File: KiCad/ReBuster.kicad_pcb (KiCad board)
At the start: 4 copper layers, 38 x 38 mm, 37 parts, among them U1 10M02SCU169, U2 LM1117-3.3, U3 SN74CBTD16210, U4 SN74LVC16T245DGVR, U5 SN74CBTD16210, U6 SN74CBTD16210, U7 74LVC2T45DC, U8 PLCC_84_plug, U9 PLCC_84_plug

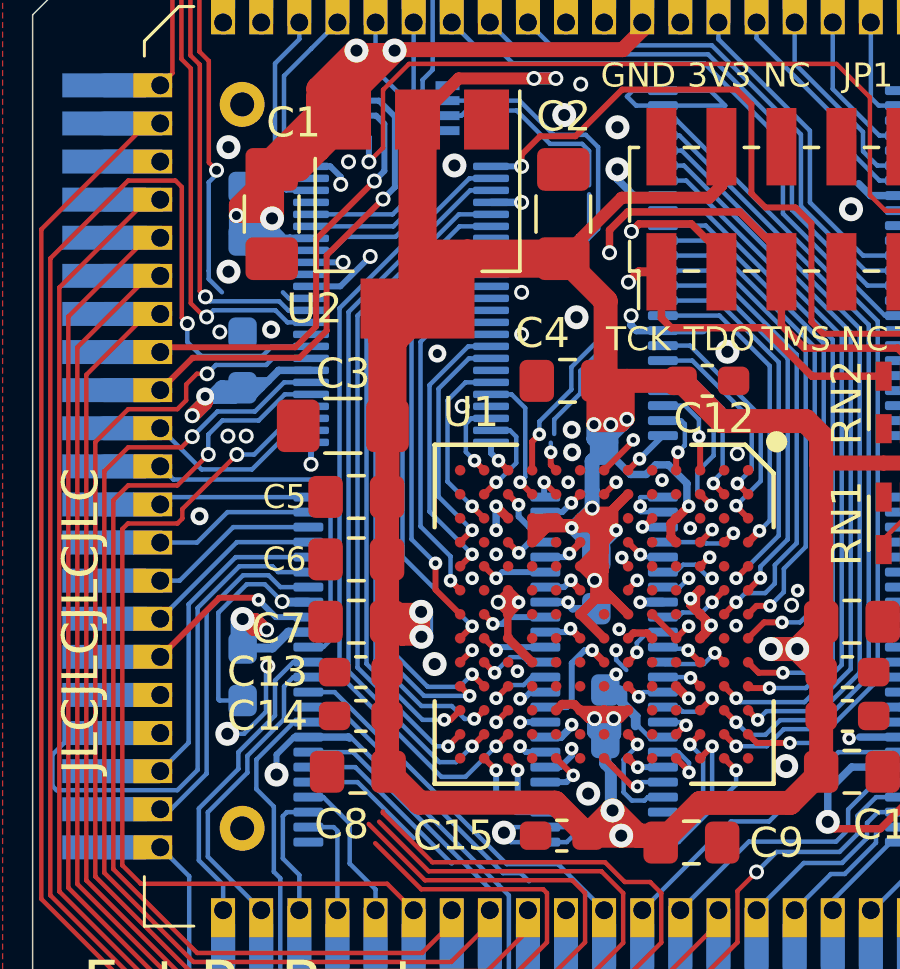
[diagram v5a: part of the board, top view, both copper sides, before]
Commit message: Route EDS0 to U4 (SN74LVC16T245DGVR) change F4 -> N8 in FPGA
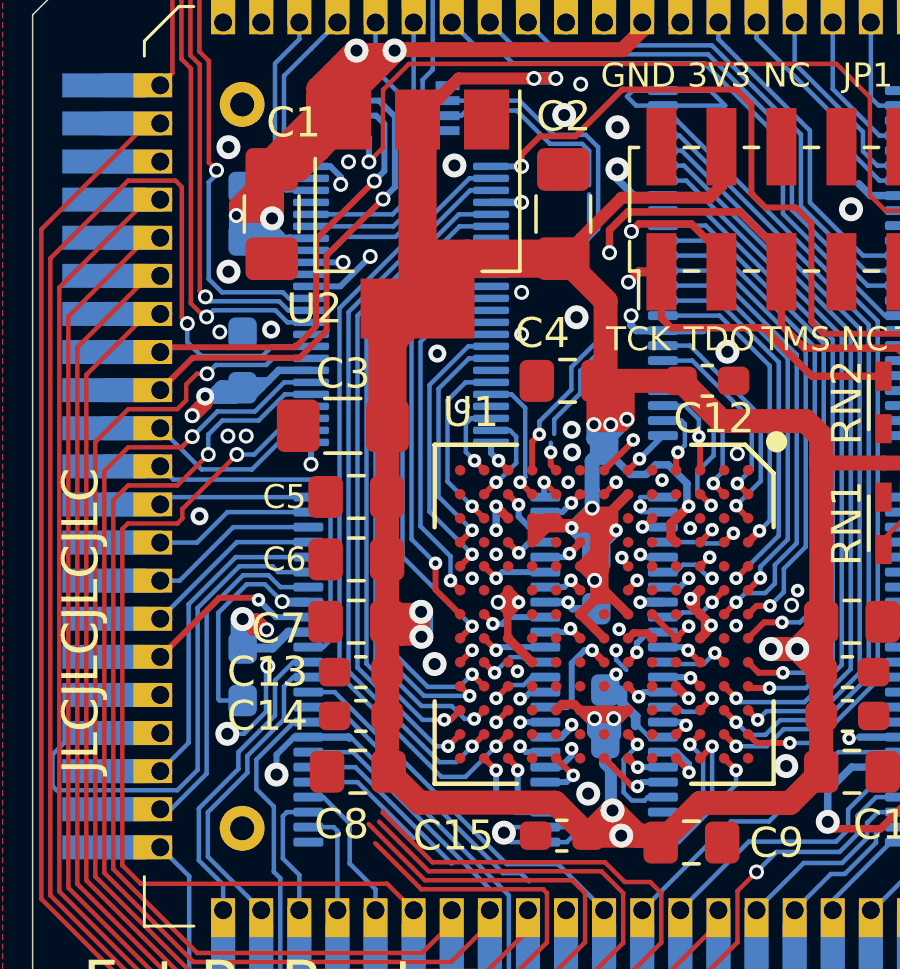
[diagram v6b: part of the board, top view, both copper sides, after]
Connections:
- U1 pad F4: EDS0_FPGA -> Net-(U1-PadF4)
- U1 pad N8: Net-(U1-PadN8) -> EDS0_FPGA
- U4 pad 13: Net-(U4-Pad13) -> EDS0
- U4 pad 36: Net-(U4-Pad36) -> EDS0_FPGA
- U5 pad 44: EDS0_FPGA -> Net-(U5-Pad44)
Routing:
- net Net-(U1-PadN8): track 13.9 -> 0.00 mm, vias 1 -> 0
- net EDS0_FPGA: track 1.36 -> 14.7 mm
- net EDS0: track 62.7 -> 65.7 mm
- net Net-(U4-Pad13): track 1.02 -> 0.00 mm
- net Net-(U5-Pad44): track 0.00 -> 0.79 mm, vias 0 -> 1

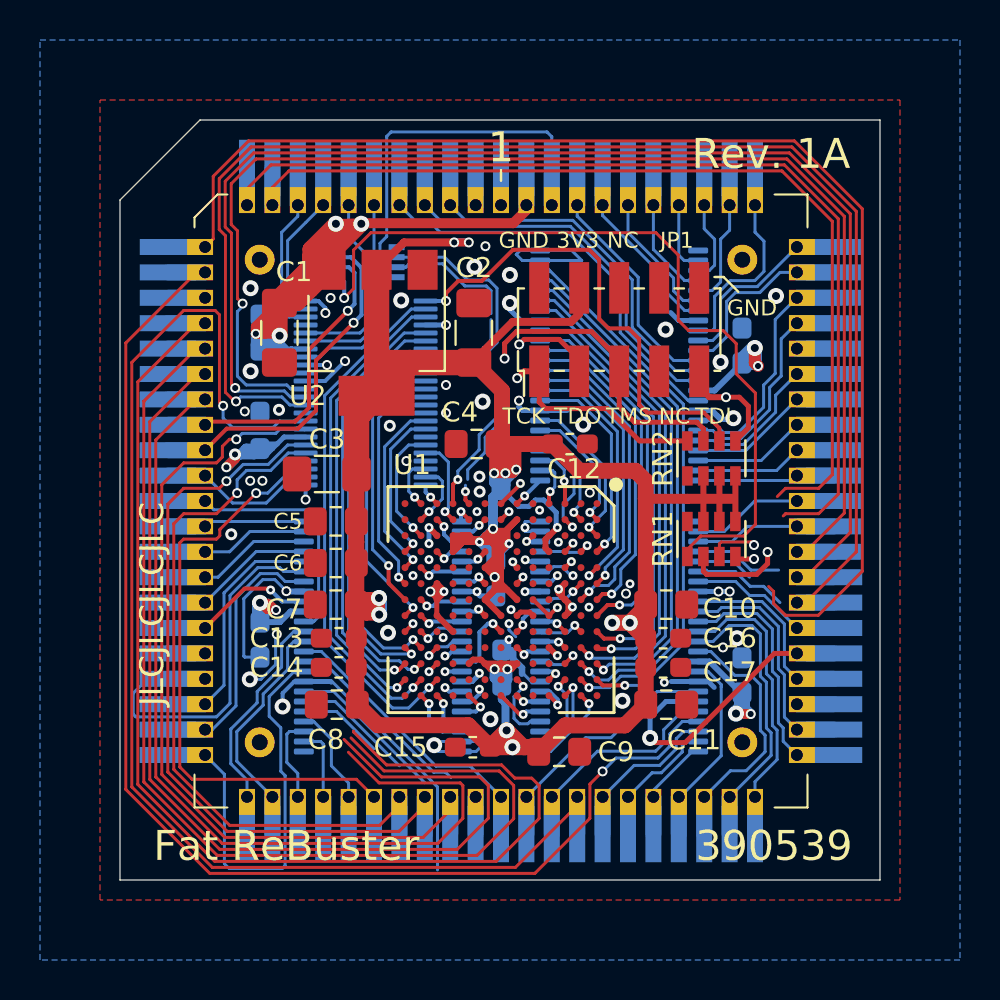
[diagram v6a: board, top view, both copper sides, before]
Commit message: Route RMC, SBR, SBG, CIIN to U6 (SN74CBTD16210) and assign pins K10, K11, K12, H13 in FPGA respectively
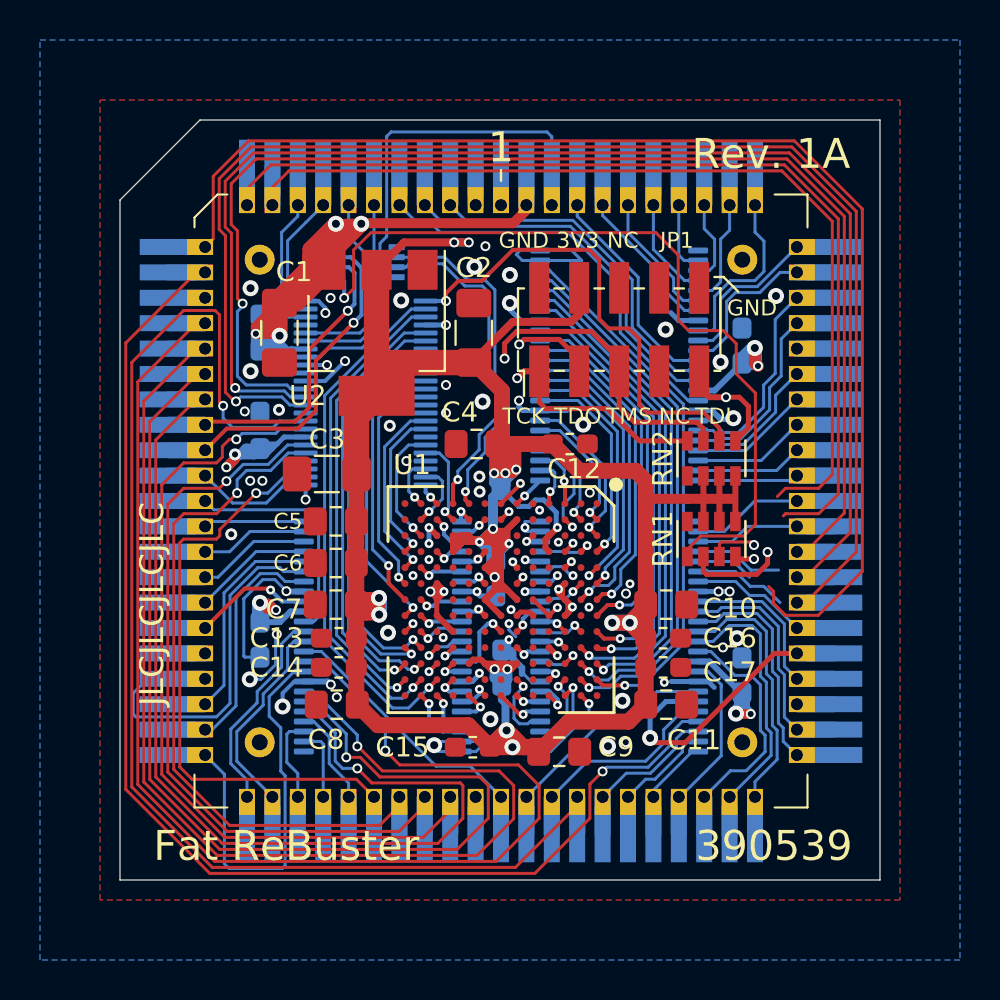
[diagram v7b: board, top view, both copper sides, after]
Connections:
- U1 pad H13: Net-(U1-PadH13) -> CIIN_FPGA
- U1 pad J1: Net-(U1-PadJ1) -> DTACK_FPGA
- U1 pad K1: Net-(U1-PadK1) -> MTACK_FPGA
- U1 pad K10: Net-(U1-PadK10) -> RMC_FPGA
- U1 pad K11: Net-(U1-PadK11) -> SBR_FPGA
- U1 pad K12: Net-(U1-PadK12) -> SBG_FPGA
- U6 pad 10: Net-(U6-Pad10) -> RMC
- U6 pad 38: Net-(U6-Pad38) -> RMC_FPGA
- U6 pad 40: Net-(U6-Pad40) -> SBR_FPGA
- U6 pad 42: Net-(U6-Pad42) -> SBG_FPGA
- U6 pad 43: Net-(U6-Pad43) -> CIIN_FPGA
- U6 pad 5: Net-(U6-Pad5) -> CIIN
- U6 pad 6: Net-(U6-Pad6) -> SBG
- U6 pad 7: Net-(U6-Pad7) -> SBR
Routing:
- net GND: track 75.7 -> 64.1 mm, vias 59 -> 62
- net Net-(U1-PadK1): track 10.7 -> 0.00 mm, vias 1 -> 0
- net MTACK_FPGA: track 6.49 -> 17.0 mm, vias 0 -> 1
- net Net-(U6-Pad10): track 9.76 -> 0.00 mm
- net Net-(U6-Pad7): track 7.94 -> 0.00 mm
- net Net-(U6-Pad6): track 6.11 -> 0.00 mm
- net RMC: track 61.2 -> 65.9 mm, vias 0 -> 1
- net Net-(U6-Pad5): track 4.28 -> 0.00 mm
- net CIIN: track 47.3 -> 51.2 mm, vias 0 -> 1
- net SBR: track 56.6 -> 60.3 mm, vias 0 -> 1
- net SBG: track 52.3 -> 55.8 mm, vias 0 -> 1
- net CIIN_FPGA: track 0.00 -> 1.71 mm, vias 0 -> 1
- net RMC_FPGA: track 0.00 -> 1.52 mm, vias 0 -> 1
- net SBG_FPGA: track 0.00 -> 1.49 mm, vias 0 -> 1
- net SBR_FPGA: track 0.00 -> 1.41 mm, vias 0 -> 1
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
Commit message: small routing fixes upgrading 0.45/0.2 mm vias to 0.5/0.3 mm where possible
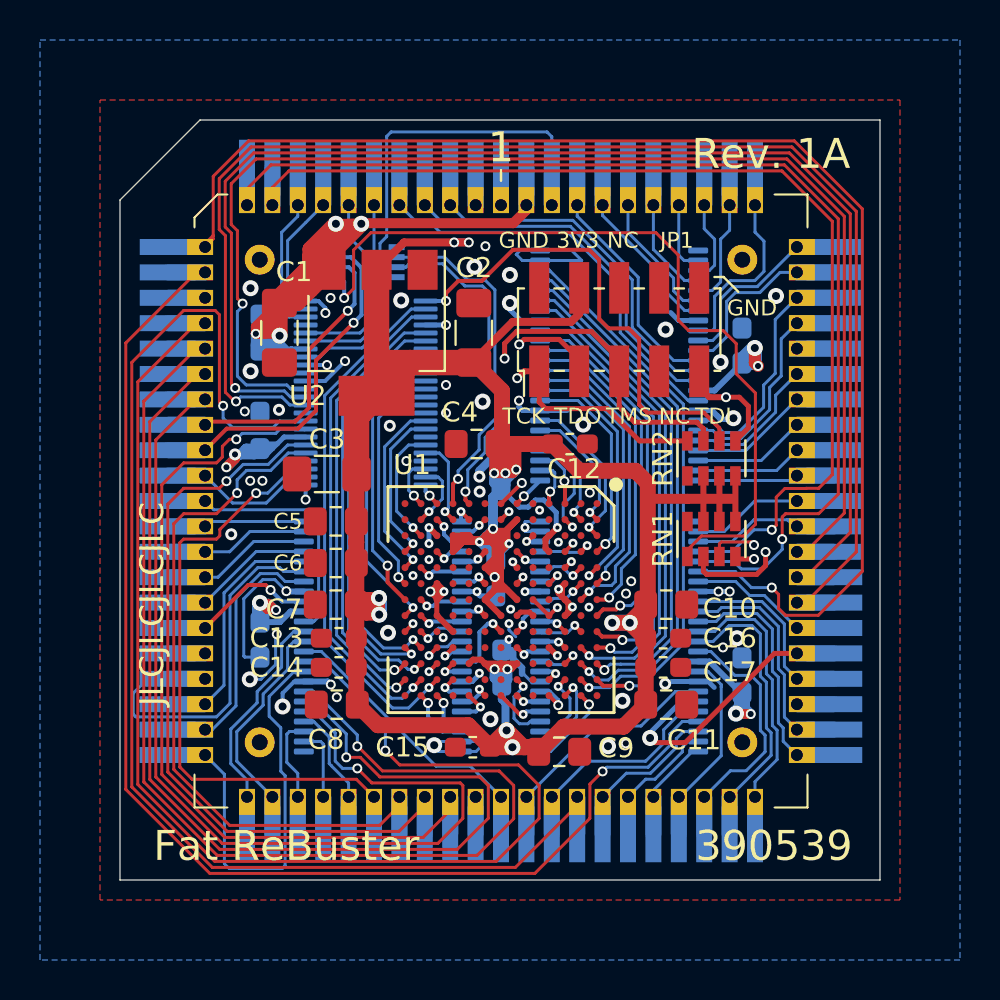
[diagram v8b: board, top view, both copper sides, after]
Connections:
- net JP1 renamed Net-(U1-PadB1)
- U1 pad B5: Net-(U1-PadB5) -> DSACK0_FPGA
- U1 pad D6: Net-(U1-PadD6) -> DSACK1_FPGA
- U1 pad F4: Net-(U1-PadF4) -> DS_FPGA
- U5 pad 4: Net-(U5-Pad4) -> DS
- U5 pad 42: Net-(U5-Pad42) -> DSACK1_FPGA
- U5 pad 43: Net-(U5-Pad43) -> DSACK0_FPGA
- U5 pad 44: Net-(U5-Pad44) -> DS_FPGA
- U5 pad 5: Net-(U5-Pad5) -> DSACK0
- U5 pad 6: Net-(U5-Pad6) -> DSACK1
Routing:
- net DSACK0: track 50.8 -> 57.3 mm, vias 0 -> 1
- net DS: track 48.0 -> 53.9 mm, vias 0 -> 1
- net Net-(U5-Pad6): track 4.73 -> 0.00 mm
- net DSACK1: track 64.8 -> 69.5 mm, vias 0 -> 1
- net Net-(U5-Pad4): track 4.41 -> 0.00 mm
- net Net-(U5-Pad5): track 2.89 -> 0.00 mm
- net DSACK0_FPGA: track 0.00 -> 2.49 mm, vias 0 -> 1
- net Net-(U5-Pad43): track 1.93 -> 0.00 mm, vias 1 -> 0
- net GND: track 64.1 -> 65.8 mm
- net DSACK1_FPGA: track 0.00 -> 1.57 mm, vias 0 -> 1
- net DS_FPGA: track 0.00 -> 1.36 mm, vias 0 -> 1
- net Net-(U5-Pad42): track 0.98 -> 0.00 mm, vias 1 -> 0
- net EBCLR: track 7.12 -> 7.99 mm
- net Net-(U5-Pad44): track 0.79 -> 0.00 mm, vias 1 -> 0
